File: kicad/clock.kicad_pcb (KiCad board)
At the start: 2 copper layers, 100 x 100 mm, 77 parts, among them Q1 PN2222A, Q2 PN2222A, Q3 PN2222A, Q4 PN2222A, Q5 PN2222A, Q6 PN2222A, SW1 SW_DIP_x08, SW2 SW_Push, SW3 SW_Push, SW4 SW_DIP_x08, U1 74HC04, U10 7SEGMENT_CC, U11 4543, U12 7SEGMENT_CC, U13 4543, U14 7SEGMENT_CC, U15 74LS390, U16 4027, U17 74HC688, U18 NE555, U19 74HC688, U2 74LS390, U3 CD4060, U4 4543, U5 7SEGMENT_CC, U6 4027, U7 74LS390, U8 74LS390, U9 4543, Y1 32768

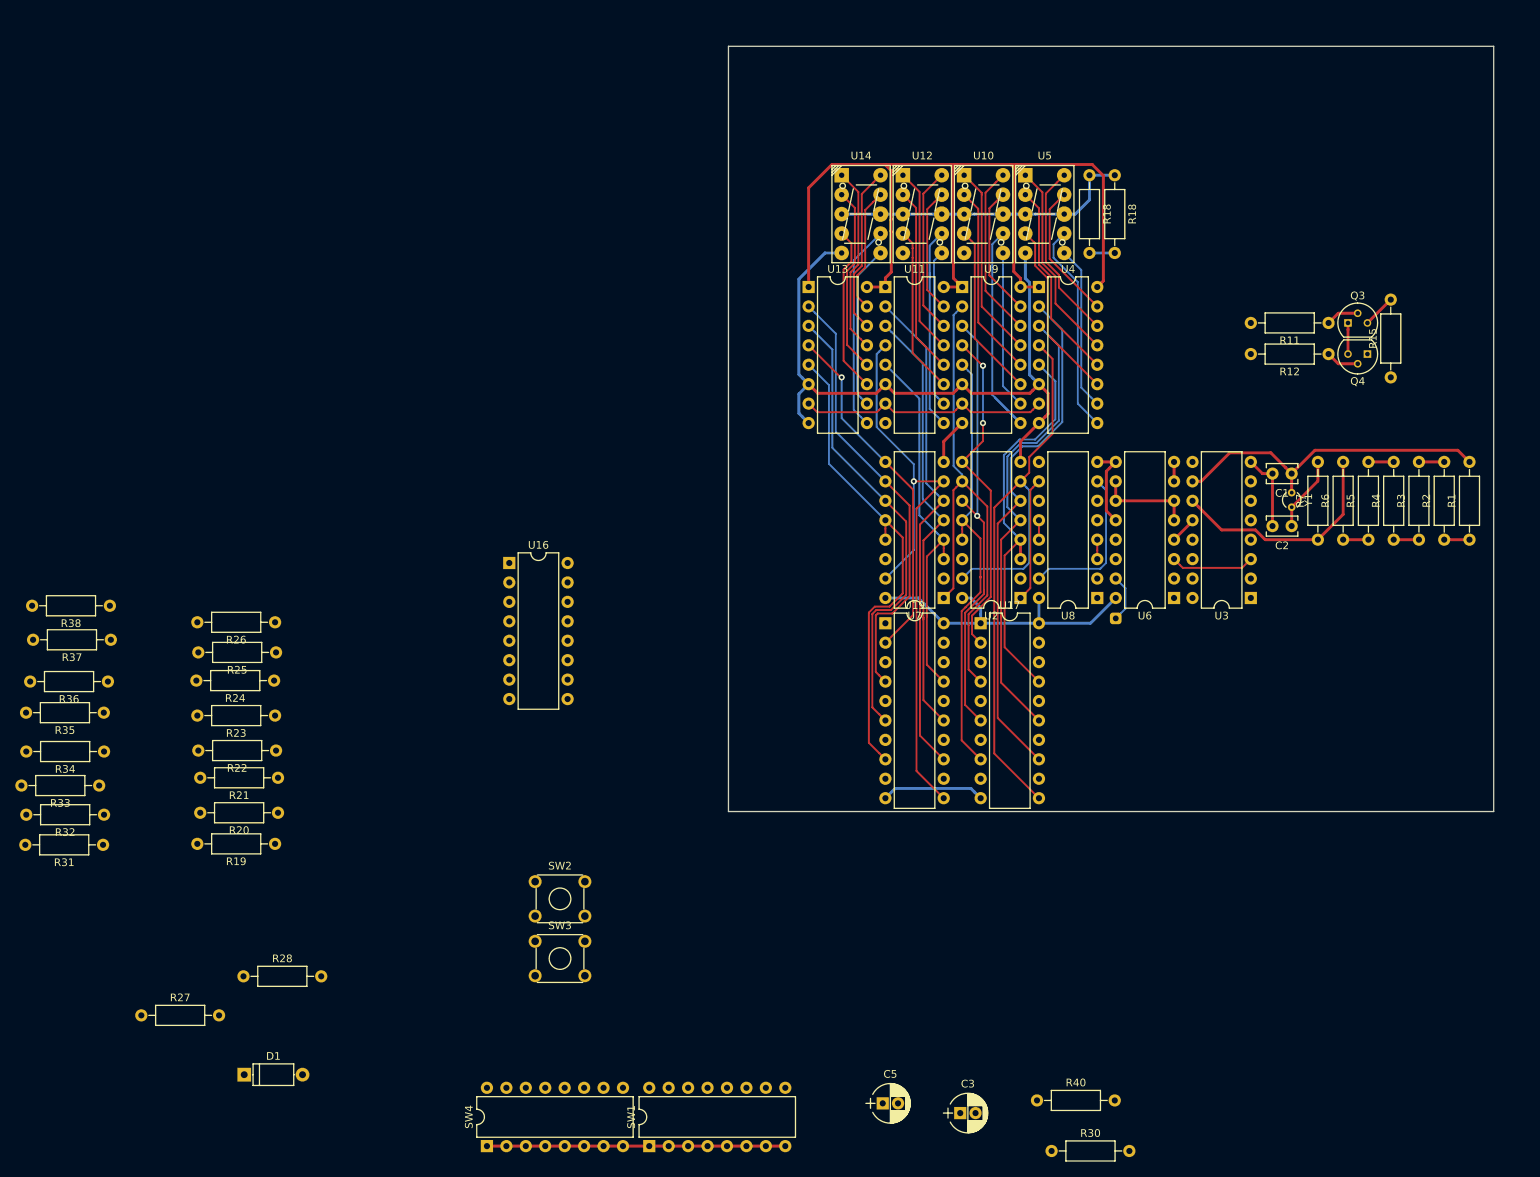
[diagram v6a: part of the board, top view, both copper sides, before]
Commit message: Routed switches
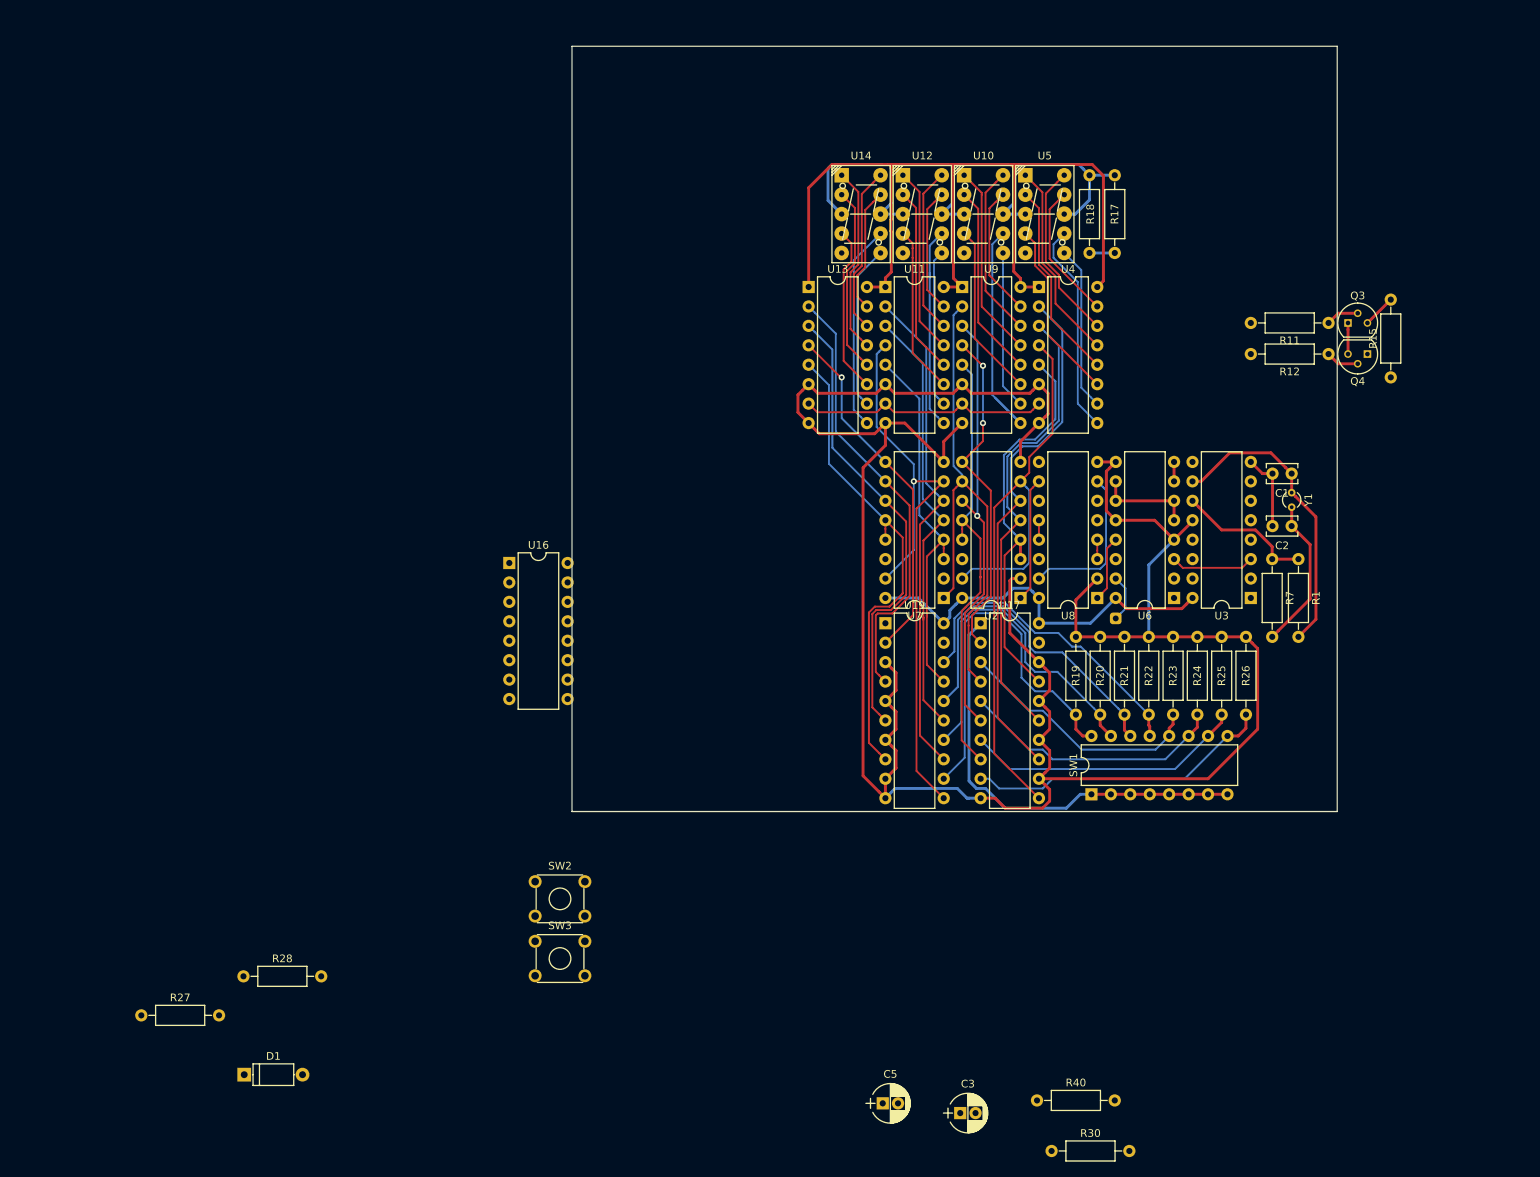
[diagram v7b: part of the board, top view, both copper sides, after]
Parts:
- removed the R18 at (165.5, 61.8)
- removed R2, R3, R4, R5, R6: 1M, Resistors_THT:R_Axial_DIN0207_L6.3mm_D2.5mm_P10.16mm_Horizontal
- removed R31, R32, R33, R34, R35, R36, R37, R38: 22k, Resistors_THT:R_Axial_DIN0207_L6.3mm_D2.5mm_P10.16mm_Horizontal
- removed SW4: SW_DIP_x08, Housings_DIP:DIP-16_W7.62mm
- added R17: 1k, Resistors_THT:R_Axial_DIN0207_L6.3mm_D2.5mm_P10.16mm_Horizontal, F.Cu at (165.5, 61.8)
- R1: value 1M -> 10M
- moved R26 126.9 mm to (182.6, 122.2), turned to 270 degrees
- moved R25 123.6 mm to (179.5, 122.2), turned to 270 degrees
- moved R24 120.8 mm to (176.3, 122.2), turned to 270 degrees
- moved R23 117.8 mm to (173.1, 122.2), turned to 270 degrees
- moved R22 115.0 mm to (169.9, 122.2), turned to 270 degrees
- moved R21 112.1 mm to (166.8, 122.2), turned to 270 degrees
- moved R20 109.9 mm to (163.6, 122.2), turned to 270 degrees
- moved R19 108.1 mm to (160.4, 122.2), turned to 270 degrees
- moved SW1 73.8 mm to (162.4, 142.7)
- moved R1 22.5 mm to (189.5, 112.0), turned to 270 degrees
- moved R7 6.49 mm to (186.1, 112.0), turned to 270 degrees
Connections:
- R7 pad 1: Net-(R6-Pad2) -> Net-(R1-Pad1)
- U10 pad 5: ALM -> (no net)
- U12 pad 5: 1Hz -> (no net)
- U14 pad 5: GND -> (no net)
- U17 pad 12: /Alarm/B4 -> GND
- U17 pad 14: /Alarm/B5 -> GND
- U17 pad 16: /Alarm/B6 -> GND
- U17 pad 18: /Alarm/B7 -> GND
- U17 pad 3: /Alarm/B0 -> /Alarm/B4
- U17 pad 5: /Alarm/B1 -> /Alarm/B5
- U17 pad 7: /Alarm/B2 -> /Alarm/B6
- U17 pad 9: /Alarm/B3 -> /Alarm/B7
- U19 pad 12: /Alarm/C4 -> /Alarm/B0
- U19 pad 14: /Alarm/C5 -> /Alarm/B1
- U19 pad 16: /Alarm/C6 -> /Alarm/B2
- U19 pad 18: /Alarm/C7 -> /Alarm/B3
- U19 pad 3: /Alarm/C0 -> GND
- U19 pad 5: /Alarm/C1 -> GND
- U19 pad 7: /Alarm/C2 -> GND
- U19 pad 9: /Alarm/C3 -> GND
- U3 pad 11: Net-(R6-Pad2) -> Net-(R1-Pad1)
- U5 pad 5: GND -> (no net)
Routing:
- net GND: track 140.8 -> 339.0 mm
- net /Alarm/B0: track 0.00 -> 49.7 mm
- net /Alarm/B1: track 0.00 -> 46.5 mm
- net Net-(R17-Pad1): track 39.7 -> 85.1 mm
- net /Alarm/B2: track 0.00 -> 44.0 mm
- net /Alarm/B3: track 0.00 -> 41.4 mm
- net /Alarm/B7: track 0.00 -> 40.2 mm
- net /Alarm/B6: track 0.00 -> 36.6 mm
- net /Alarm/B5: track 0.00 -> 34.9 mm
- net /Alarm/B4: track 0.00 -> 33.1 mm
- net Net-(R6-Pad2): track 30.0 -> 0.00 mm
- net VCC: track 219.6 -> 248.4 mm
- net Net-(R1-Pad1): track 3.30 -> 17.9 mm
- net Net-(C2-Pad1): track 9.80 -> 20.0 mm
- net 1Hz: track 0.00 -> 8.62 mm
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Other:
- board text removed: "FIXME: 7-SEGMENT DISPLAYS ARE BACKWARDS!"

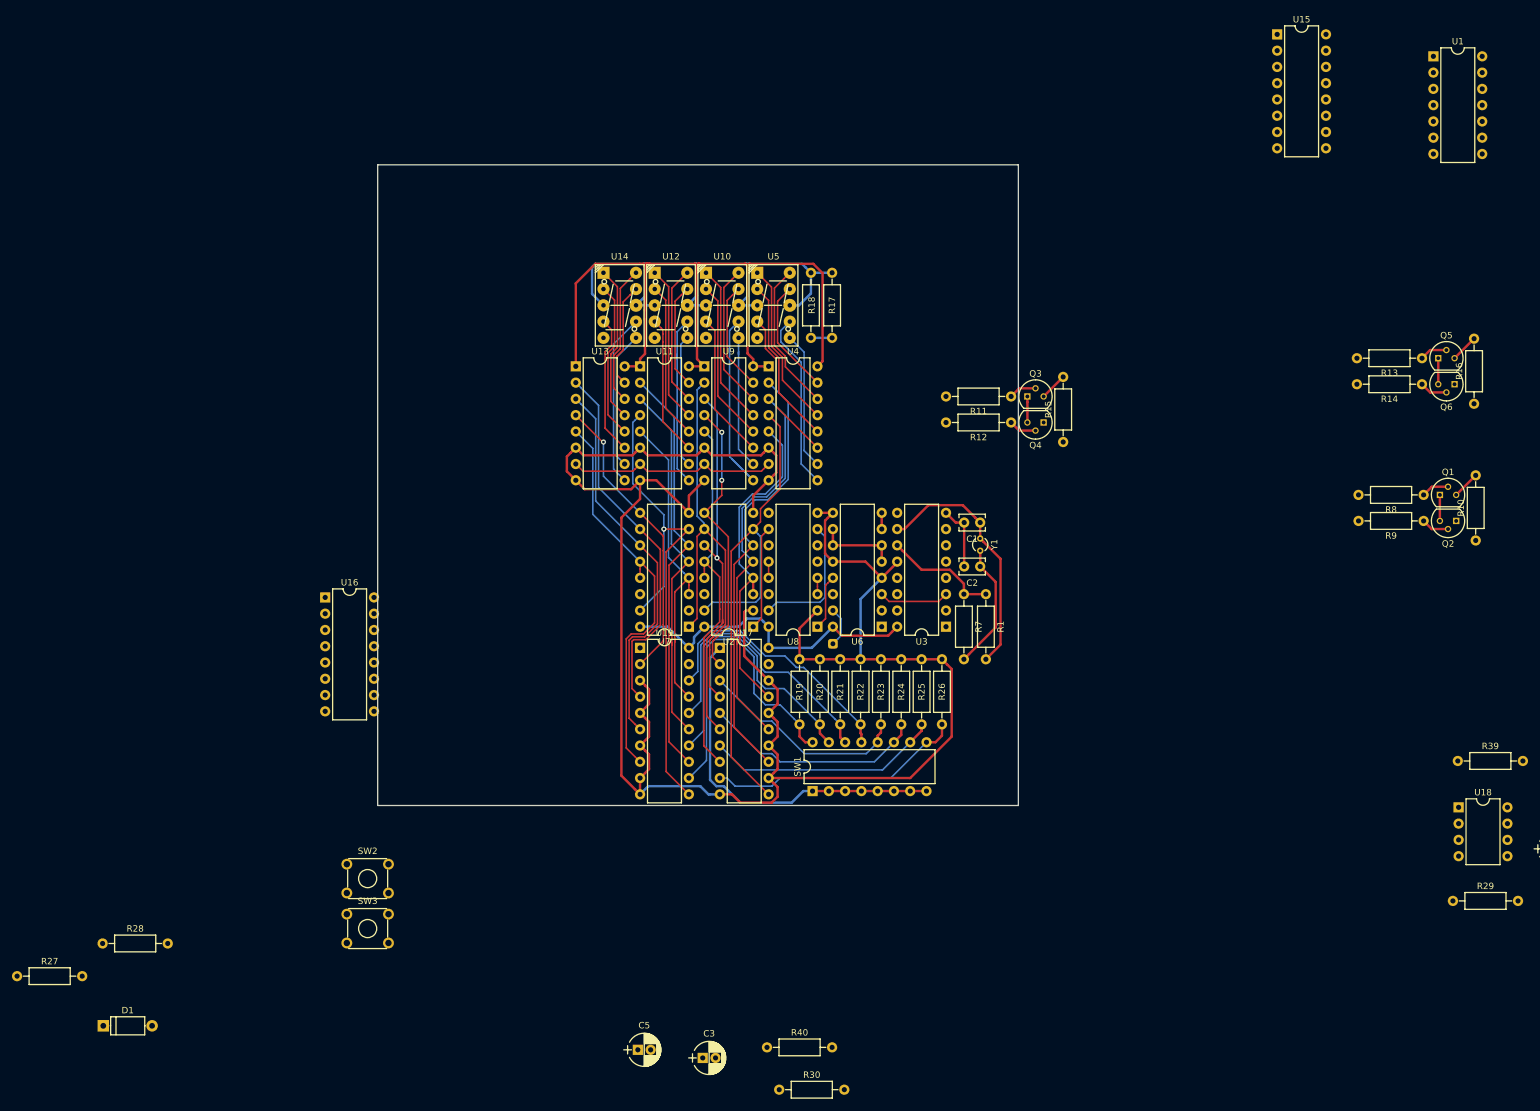
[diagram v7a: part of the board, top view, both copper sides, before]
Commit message: Corrected schematic: SET button and discrete NAND blob
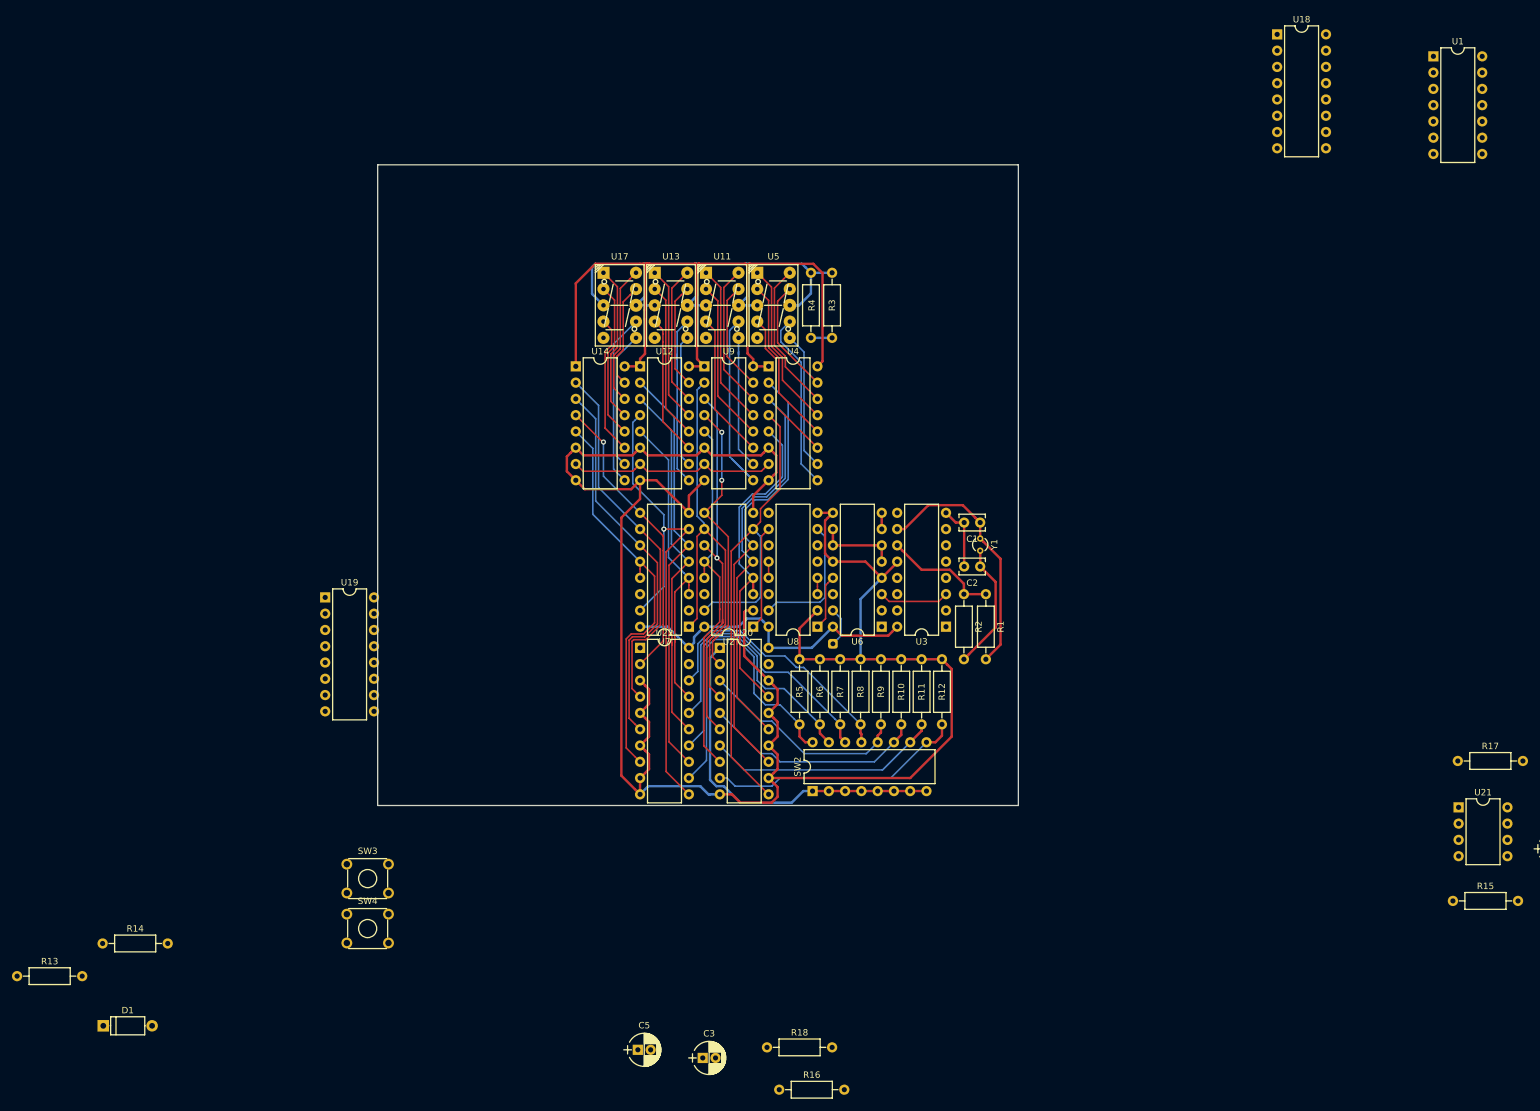
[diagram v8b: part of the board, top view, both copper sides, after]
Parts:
- removed Q1, Q2, Q3, Q4, Q5, Q6: PN2222A, TO_SOT_Packages_THT:TO-92_Molded_Narrow
- removed the R10 at (265.9, 103.6)
- removed the R11 at (193.4, 81.2)
- removed the R12 at (193.4, 85.2)
- removed the R13 at (257.6, 75.2)
- removed the R14 at (257.6, 79.2)
- removed the R15 at (201.5, 88.3)
- removed the R16 at (265.7, 82.3)
- removed the R8 at (257.8, 96.5)
- removed the R9 at (257.8, 100.6)
- renumbered R24 to R10, R25 to R11, R26 to R12, R27 to R13, R28 to R14, R29 to R15, R30 to R16, R39 to R17, R40 to R18, R7 to R2, R17 to R3, R18 to R4, R19 to R5, R20 to R6, R21 to R7, R22 to R8, R23 to R9, SW1 to SW2, SW2 to SW3, SW3 to SW4, U10 to U11, U11 to U12, U12 to U13, U13 to U14, U14 to U17, U15 to U18, U16 to U19, U17 to U20, U18 to U21, U19 to U22
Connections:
- U1 pad 1: Net-(Q1-Pad3) -> (no net)
- U1 pad 3: Net-(Q5-Pad3) -> (no net)
- U1 pad 5: Net-(Q3-Pad3) -> (no net)
- U8 pad 11: Net-(R11-Pad2) -> (no net)
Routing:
- net Net-(Q3-Pad2): track 4.34 -> 0.00 mm
- net Net-(Q2-Pad2): track 4.34 -> 0.00 mm
- net Net-(Q1-Pad2): track 4.34 -> 0.00 mm
- net Net-(Q4-Pad2): track 4.34 -> 0.00 mm
- net Net-(Q6-Pad2): track 4.34 -> 0.00 mm
- net Net-(Q5-Pad2): track 4.34 -> 0.00 mm
- net Net-(Q5-Pad3): track 4.31 -> 0.00 mm
- net Net-(Q3-Pad3): track 4.31 -> 0.00 mm
- net Net-(Q1-Pad3): track 4.31 -> 0.00 mm
- net Net-(Q5-Pad1): track 4.06 -> 0.00 mm
- net Net-(Q1-Pad1): track 4.06 -> 0.00 mm
- net Net-(Q3-Pad1): track 4.06 -> 0.00 mm
